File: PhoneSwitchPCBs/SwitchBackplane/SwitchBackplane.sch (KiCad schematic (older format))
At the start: 13 parts

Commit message: Continue work on backplane schematic
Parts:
- added C? (x4): .33u, symbol Device:C_Small
- added C? (x2): .22u, symbol Device:C_Small
- added C? (x2): .1u, symbol Device:C_Small
- added D? (x6): 1N4148, Diode_THT:D_DO-35_SOD27_P7.62mm_Horizontal, symbol Diode:1N4148
- added R? (x3): 4.7k, symbol Device:R_Small
- added R? (x3): 2.2k, symbol Device:R_Small
- added R? (x2): 1.1k, symbol Device:R_Small
- added R? (x2): 1.0k, symbol Device:R_Small
- added R? (x2): 1.17k, symbol Device:R_Small
- added R? (x4): 100k, symbol Device:R_Small
- added U? (x4): 74HC4066, Package_SO:SO-14_3.9x8.65mm_P1.27mm, symbol SwitchBackplaneParts:74HC4066
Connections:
- net labels added: +5V, -5V
- wire segments 29 -> 143
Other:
- moved on the sheet: C?, R?, U?A, U?B, U?C, U?D, U?E

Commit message: Added simulation of tone generators, updated backplane schematic
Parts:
- removed U? (x4): 74HC4066, Package_SO:SO-14_3.9x8.65mm_P1.27mm, symbol SwitchBackplaneParts:74HC4066
- added C? (x2): .1u, symbol Device:C_Small
- added R?: 100k, symbol Device:R_Small
- added R?: 470k, symbol Device:RTRIM
- added U? (x5): 74HC4316, symbol SwitchBackplaneParts:74HC4316
- added U?: TL071, symbol SwitchBackplaneParts:TL071
- C? (x2): value .68u -> .1u
- C? (x4): value .33u -> .1u
- C? (x2): value .22u -> .1u
- R? (x2): value 680 -> 4.53k
- R? (x2): value 1.1k -> 3.6k
- R? (x2): value 1.0k -> 3.32k
- R? (x2): value 1.17k -> 2.55k
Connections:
- wire segments 143 -> 169
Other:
- moved on the sheet: C?, R?, U?A, U?B, U?C, U?D

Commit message: Continued work on backplane schematic
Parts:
- removed D? (x8): 1N4148, Diode_THT:D_DO-35_SOD27_P7.62mm_Horizontal, symbol Diode:1N4148
- added C? (x16): .1u, symbol Device:C_Small
- added D? (x8): PMBD7000, Package_TO_SOT_SMD:SOT-23, symbol SwitchBackplaneParts:PMBD7000
- added J?: Station 1, symbol Connector_Generic:Conn_02x11_Odd_Even
- added R? (x5): 100k, symbol Device:R_Small
- added R? (x2): 2.55k, symbol Device:R_Small
- added R? (x4): 2.2k, symbol Device:R_Small
- added R? (x4): 4.7k, symbol Device:R_Small
- added R? (x2): 3.32k, symbol Device:R_Small
- added R? (x2): 3.6k, symbol Device:R_Small
- added R? (x2): 4.53k, symbol Device:R_Small
- added R?: 500k, symbol Device:RTRIM
- added U? (x5): TL074, symbol Amplifier_Operational:TL074
- added U? (x5): 74HC4316, symbol SwitchBackplaneParts:74HC4316
- added U?: TL071, symbol SwitchBackplaneParts:TL071
- R?: value 470k -> 500k
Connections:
- net labels added: +3.3V, +5VA, +5VD, -48V, -5VA
- net labels removed: +5V, -5V
- wire segments 169 -> 350
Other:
- note added: "Call-Progress Tone Generators"
- moved on the sheet: C?, R?, U?, U?A, U?B, U?C, U?D, U?E

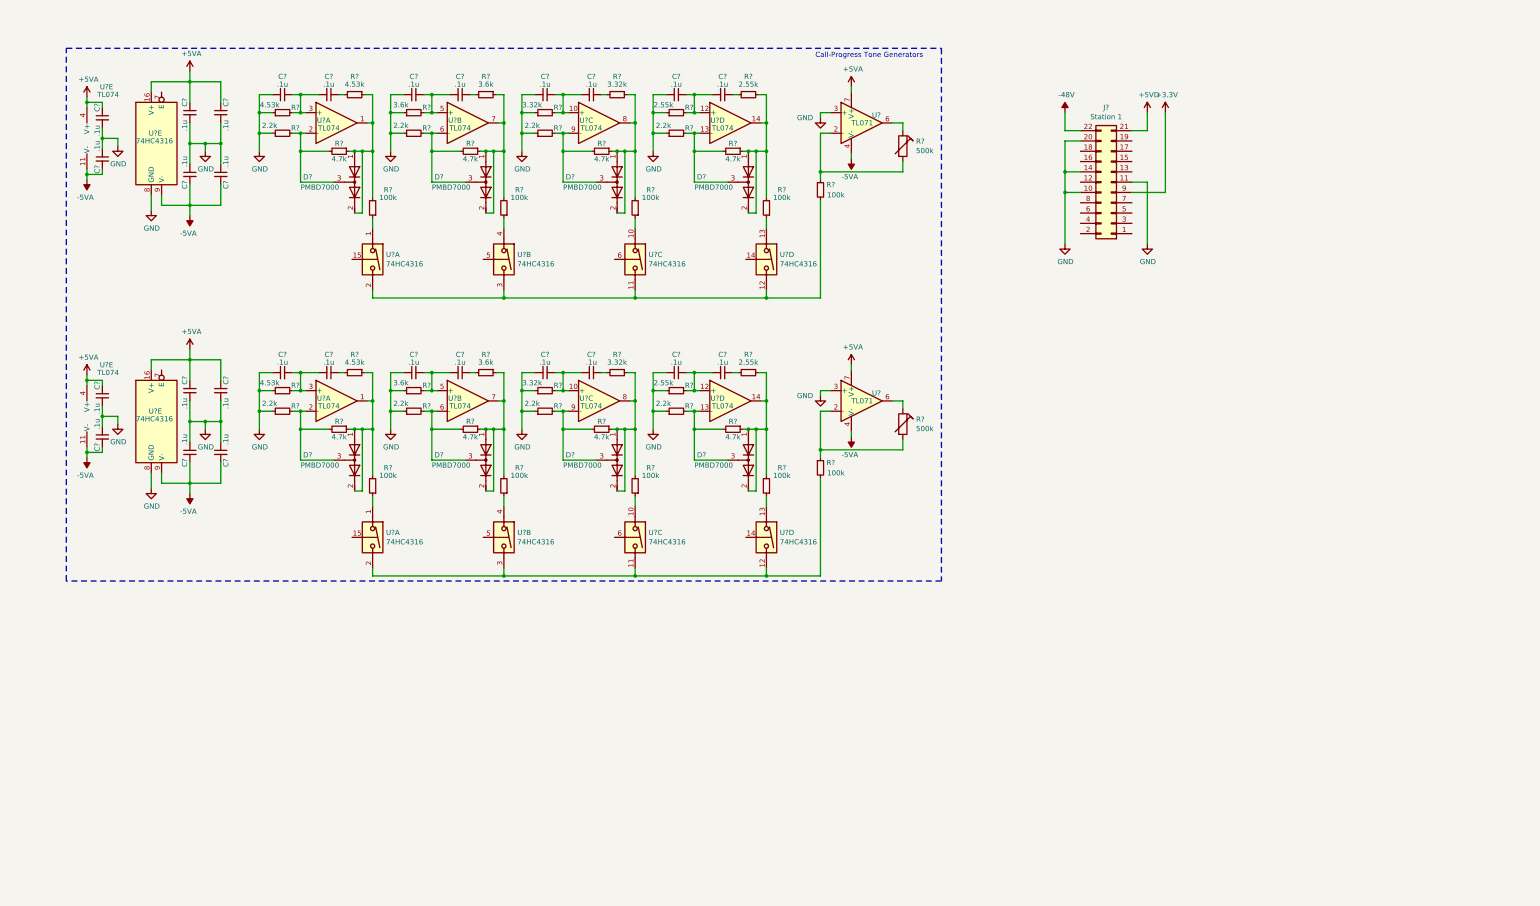
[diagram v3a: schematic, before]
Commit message: Add station interface ports, initial power supply design
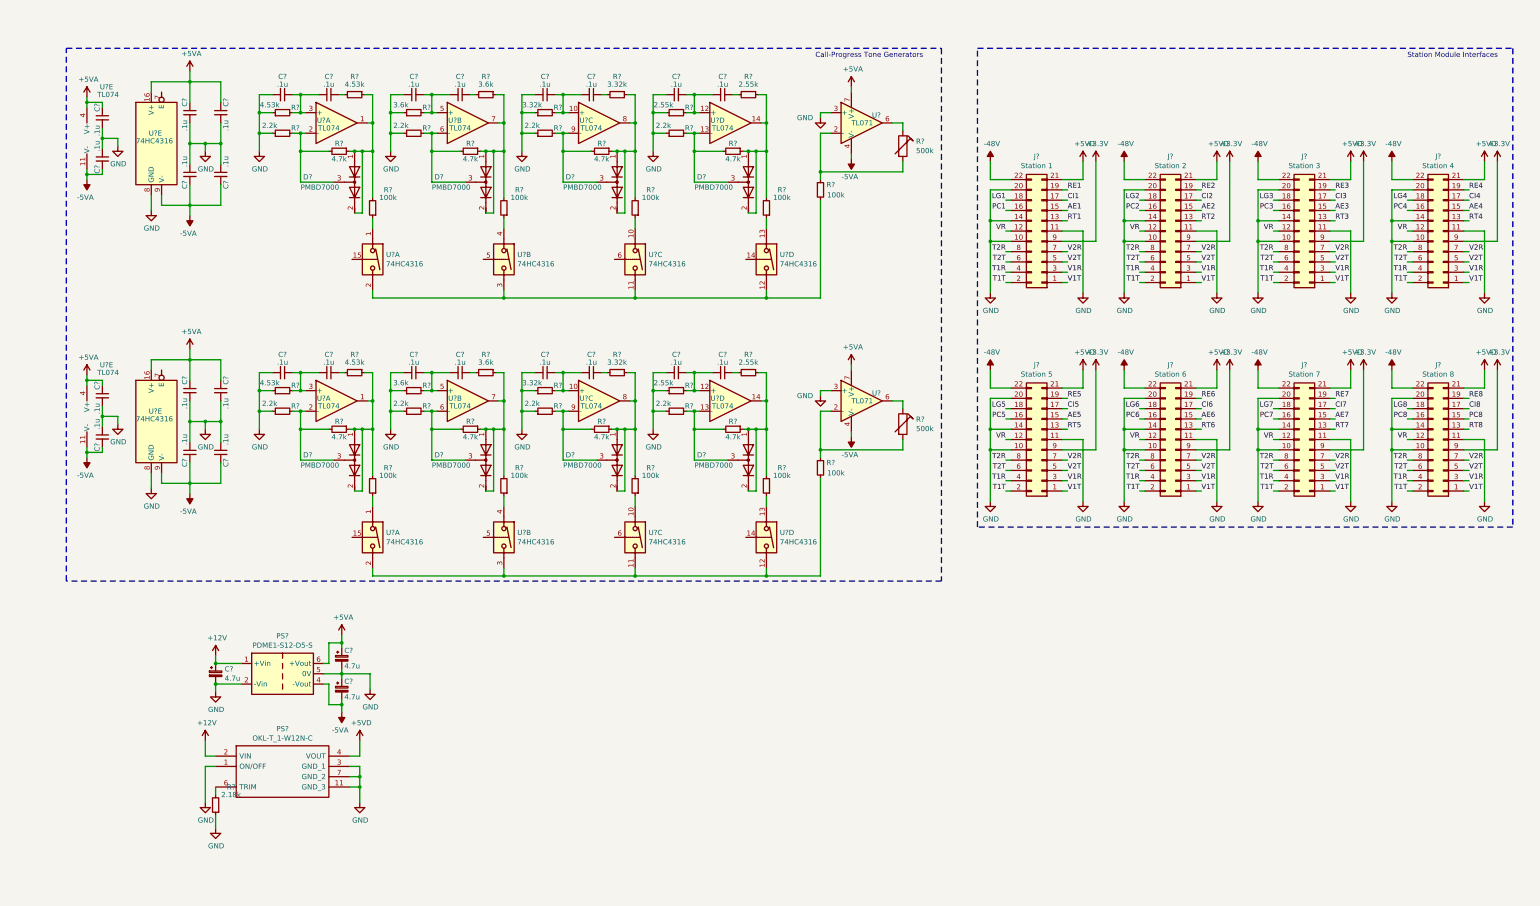
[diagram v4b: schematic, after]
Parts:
- added C? (x3): 4.7u, symbol Device:CP_Small
- added J?: Station 2, symbol Connector_Generic:Conn_02x11_Odd_Even
- added J?: Station 3, symbol Connector_Generic:Conn_02x11_Odd_Even
- added J?: Station 4, symbol Connector_Generic:Conn_02x11_Odd_Even
- added J?: Station 5, symbol Connector_Generic:Conn_02x11_Odd_Even
- added J?: Station 6, symbol Connector_Generic:Conn_02x11_Odd_Even
- added J?: Station 7, symbol Connector_Generic:Conn_02x11_Odd_Even
- added J?: Station 8, symbol Connector_Generic:Conn_02x11_Odd_Even
- added PS?: PDME1-S12-D5-S, symbol SwitchBackplaneParts:PDME1-S12-D5-S
- added PS?: OKL-T_1-W12N-C, OKLT1W12NC, symbol Imported_Parts:OKL-T_1-W12N-C
- added R?: 2.18k, symbol Device:R_Small
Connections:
- net +3V3: now also J?.9 (Pin_9), J?.9 (Pin_9), J?.9 (Pin_9), J?.9 (Pin_9), J?.9 (Pin_9), J?.9 (Pin_9), J?.9 (Pin_9)
- net +5VA: now also C?.1, PS?.6 (+Vout)
- net +5VD: now also J?.21 (Pin_21), J?.21 (Pin_21), J?.21 (Pin_21), J?.21 (Pin_21), J?.21 (Pin_21), J?.21 (Pin_21), J?.21 (Pin_21), PS?.4 (VOUT)
- net -48V: now also J?.22 (Pin_22), J?.22 (Pin_22), J?.22 (Pin_22), J?.22 (Pin_22), J?.22 (Pin_22), J?.22 (Pin_22), J?.22 (Pin_22)
- net -5VA: now also C?.2, PS?.4 (-Vout)
- net GND: now also C?.1, C?.2, C?.2, J?.10 (Pin_10), J?.10 (Pin_10), J?.10 (Pin_10), J?.10 (Pin_10), J?.10 (Pin_10), J?.10 (Pin_10), J?.10 (Pin_10), J?.11 (Pin_11), J?.11 (Pin_11), J?.11 (Pin_11), J?.11 (Pin_11), J?.11 (Pin_11), J?.11 (Pin_11), J?.11 (Pin_11), J?.14 (Pin_14), J?.14 (Pin_14), J?.14 (Pin_14), J?.14 (Pin_14), J?.14 (Pin_14), J?.14 (Pin_14), J?.14 (Pin_14), J?.20 (Pin_20), J?.20 (Pin_20), J?.20 (Pin_20), J?.20 (Pin_20), J?.20 (Pin_20), J?.20 (Pin_20), J?.20 (Pin_20), PS?.1 (ON/OFF), PS?.11 (GND_3), PS?.2 (-Vin), PS?.3 (GND_1), PS?.5 (0V), PS?.7 (GND_2), R?.1
- net V1T: now reaches J?.1 (Pin_1)
- net V1T: now also J?.1 (Pin_1), J?.1 (Pin_1), J?.1 (Pin_1), J?.1 (Pin_1), J?.1 (Pin_1), J?.1 (Pin_1), J?.1 (Pin_1)
- net VR: now reaches J?.12 (Pin_12)
- net VR: now also J?.12 (Pin_12), J?.12 (Pin_12), J?.12 (Pin_12), J?.12 (Pin_12), J?.12 (Pin_12), J?.12 (Pin_12), J?.12 (Pin_12)
- net RT1: now reaches J?.13 (Pin_13)
- net AE1: now reaches J?.15 (Pin_15)
- net PC1: now reaches J?.16 (Pin_16)
- net CI1: now reaches J?.17 (Pin_17)
- net LG1: now reaches J?.18 (Pin_18)
- net RE1: now reaches J?.19 (Pin_19)
- net T1T: now reaches J?.2 (Pin_2)
- net T1T: now also J?.2 (Pin_2), J?.2 (Pin_2), J?.2 (Pin_2), J?.2 (Pin_2), J?.2 (Pin_2), J?.2 (Pin_2), J?.2 (Pin_2)
- net V1R: now reaches J?.3 (Pin_3)
- net V1R: now also J?.3 (Pin_3), J?.3 (Pin_3), J?.3 (Pin_3), J?.3 (Pin_3), J?.3 (Pin_3), J?.3 (Pin_3), J?.3 (Pin_3)
- net T1R: now reaches J?.4 (Pin_4)
- net T1R: now also J?.4 (Pin_4), J?.4 (Pin_4), J?.4 (Pin_4), J?.4 (Pin_4), J?.4 (Pin_4), J?.4 (Pin_4), J?.4 (Pin_4)
- net V2T: now reaches J?.5 (Pin_5)
- net V2T: now also J?.5 (Pin_5), J?.5 (Pin_5), J?.5 (Pin_5), J?.5 (Pin_5), J?.5 (Pin_5), J?.5 (Pin_5), J?.5 (Pin_5)
- net T2T: now reaches J?.6 (Pin_6)
- net T2T: now also J?.6 (Pin_6), J?.6 (Pin_6), J?.6 (Pin_6), J?.6 (Pin_6), J?.6 (Pin_6), J?.6 (Pin_6), J?.6 (Pin_6)
- net V2R: now reaches J?.7 (Pin_7)
- net V2R: now also J?.7 (Pin_7), J?.7 (Pin_7), J?.7 (Pin_7), J?.7 (Pin_7), J?.7 (Pin_7), J?.7 (Pin_7), J?.7 (Pin_7)
- net T2R: now reaches J?.8 (Pin_8)
- net T2R: now also J?.8 (Pin_8), J?.8 (Pin_8), J?.8 (Pin_8), J?.8 (Pin_8), J?.8 (Pin_8), J?.8 (Pin_8), J?.8 (Pin_8)
- new net: PS?.6 (TRIM), R?.2
- new net +12V: C?.1, PS?.1 (+Vin), PS?.2 (VIN)
- new net AE2: J?.15 (Pin_15)
- new net AE3: J?.15 (Pin_15)
- new net AE4: J?.15 (Pin_15)
- new net AE5: J?.15 (Pin_15)
- new net AE6: J?.15 (Pin_15)
- new net AE7: J?.15 (Pin_15)
- new net CI2: J?.17 (Pin_17)
- new net CI3: J?.17 (Pin_17)
- new net CI4: J?.17 (Pin_17)
- new net CI5: J?.17 (Pin_17)
- new net CI6: J?.17 (Pin_17)
- new net CI7: J?.17 (Pin_17)
- new net CI8: J?.17 (Pin_17)
- new net LG2: J?.18 (Pin_18)
- new net LG3: J?.18 (Pin_18)
- new net LG4: J?.18 (Pin_18)
- new net LG5: J?.18 (Pin_18)
- new net LG6: J?.18 (Pin_18)
- new net LG7: J?.18 (Pin_18)
- new net LG8: J?.18 (Pin_18)
- new net PC2: J?.16 (Pin_16)
- new net PC3: J?.16 (Pin_16)
- new net PC4: J?.16 (Pin_16)
- new net PC5: J?.16 (Pin_16)
- new net PC6: J?.16 (Pin_16)
- new net PC7: J?.16 (Pin_16)
- new net PC8: J?.15 (Pin_15), J?.16 (Pin_16)
- new net RE2: J?.19 (Pin_19)
- new net RE3: J?.19 (Pin_19)
- new net RE4: J?.19 (Pin_19)
- new net RE5: J?.19 (Pin_19)
- new net RE6: J?.19 (Pin_19)
- new net RE7: J?.19 (Pin_19)
- new net RE8: J?.19 (Pin_19)
- new net RT2: J?.13 (Pin_13)
- new net RT3: J?.13 (Pin_13)
- new net RT4: J?.13 (Pin_13)
- new net RT5: J?.13 (Pin_13)
- new net RT6: J?.13 (Pin_13)
- new net RT7: J?.13 (Pin_13)
- new net RT8: J?.13 (Pin_13)
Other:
- note added: "Station Module Interfaces"
- moved on the sheet: J?

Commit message: Update notes on ring generator and continued schematic work
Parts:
- added C? (x2): 1u, symbol Device:C_Small
- added D? (x2): V3FM12, Diode_SMD:D_SMF, symbol SwitchBackplaneParts:V3FM12
- added F?: 3A, symbol Device:Fuse
- added F?: 0.5A, symbol Device:Fuse
- added F?: 150mA, symbol Device:Fuse
- added J?: Power, symbol Connector:Screw_Terminal_01x04
- added T?: FS28-200-C2, symbol SwitchBackplaneParts:FS28-200-C2
- added U?: BU33SD5, Package_TO_SOT_SMD:SOT-23-5, symbol SwitchBackplaneParts:BU33SD5
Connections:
- net +12V: now also D?.1 (K)
- net +3V3: now also C?.1, U?.5 (VOUT)
- net +5VD: now also C?.1, U?.1 (VIN), U?.3 (STBY)
- net -48V: now also D?.2 (A), F?.2
- net GND: now also R?.2, C?.2, C?.2, J?.2 (Pin_2), J?.3 (Pin_3), U?.2 (GND); no longer R?.1
- net VR: now also T?.1 (PA)
- net at PS?.6 (TRIM): now also R?.1; no longer R?.2
- new net: F?.2, J?.1 (Pin_1)
- new net: F?.2, J?.4 (Pin_4)
- new net: D?.2 (A), F?.1
- new net: D?.1 (K), F?.1
- new net: T?.2 (PA), T?.3 (PB)
- new net: F?.1, T?.4 (PB)
- new net: T?.6 (SA), T?.7 (SB)
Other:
- note added: "Power Supplies"
- moved on the sheet: C?, PS?, R?

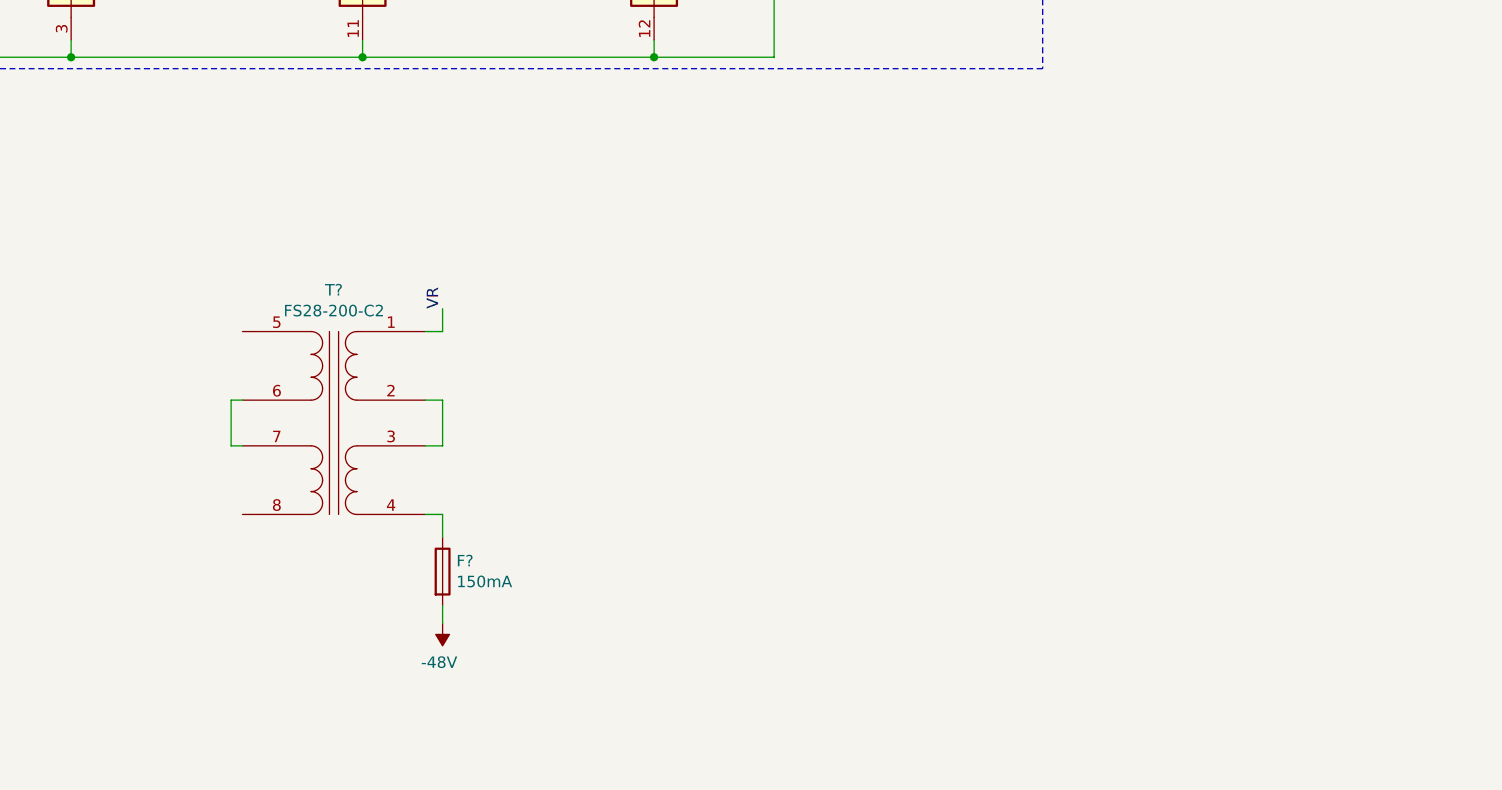
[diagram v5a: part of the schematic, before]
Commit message: Continued backplane schematic work
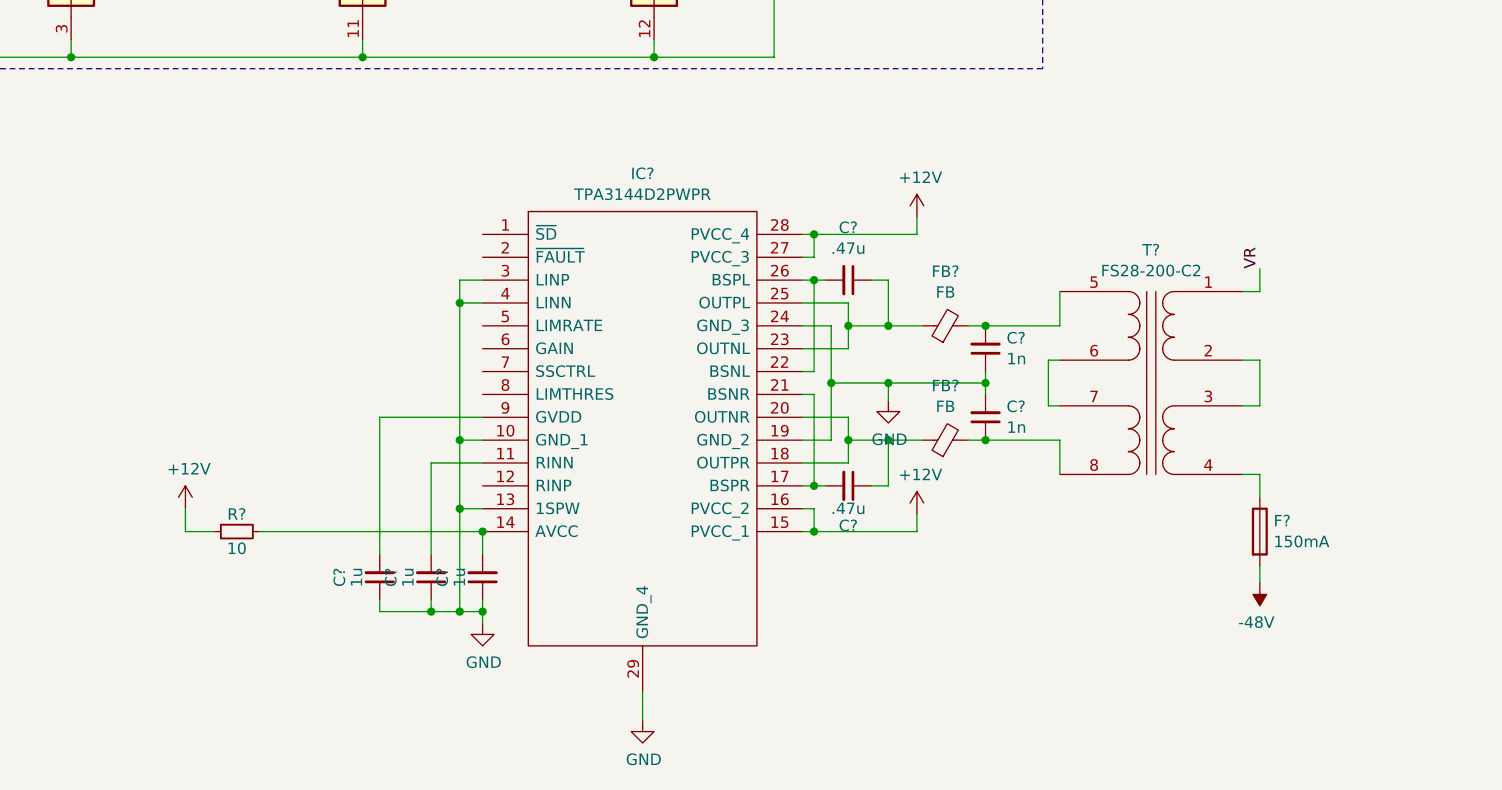
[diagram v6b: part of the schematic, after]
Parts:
- added C? (x2): .47u, symbol Device:C_Small
- added C? (x2): 1n, symbol Device:C_Small
- added C? (x3): 1u, symbol Device:C_Small
- added FB? (x2): FB, symbol Device:Ferrite_Bead_Small
- added IC?: TPA3144D2PWPR, Package_SO:HTSSOP-28-1EP_4.4x9.7mm_P0.65mm_EP2.85x5.4mm_ThermalVias, symbol SwitchBackplaneParts:TPA3144D2PWPR
- added R?: 10, symbol Device:R_Small
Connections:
- net +12V: now also IC?.15 (PVCC_1), IC?.16 (PVCC_2), IC?.27 (PVCC_3), IC?.28 (PVCC_4), R?.1
- net GND: now also C?.1, C?.1, C?.1, C?.1, C?.2, IC?.10 (GND_1), IC?.13 (1SPW), IC?.19 (GND_2), IC?.24 (GND_3), IC?.29 (GND_4), IC?.3 (LINP), IC?.4 (LINN)
- net at T?.5 (SA): now also C?.2, FB?.2
- net at T?.8 (SB): now also C?.1, FB?.2
- new net: C?.2, IC?.11 (RINN)
- new net: C?.2, IC?.14 (AVCC), R?.2
- new net: C?.2, IC?.17 (BSPR), IC?.21 (BSNR)
- new net: C?.1, FB?.1, IC?.18 (OUTPR), IC?.20 (OUTNR)
- new net: C?.2, IC?.22 (BSNL), IC?.26 (BSPL)
- new net: C?.1, FB?.1, IC?.23 (OUTNL), IC?.25 (OUTPL)
- new net: C?.2, IC?.9 (GVDD)
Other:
- moved on the sheet: F?, T?
